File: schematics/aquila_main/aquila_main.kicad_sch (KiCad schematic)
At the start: 126 parts

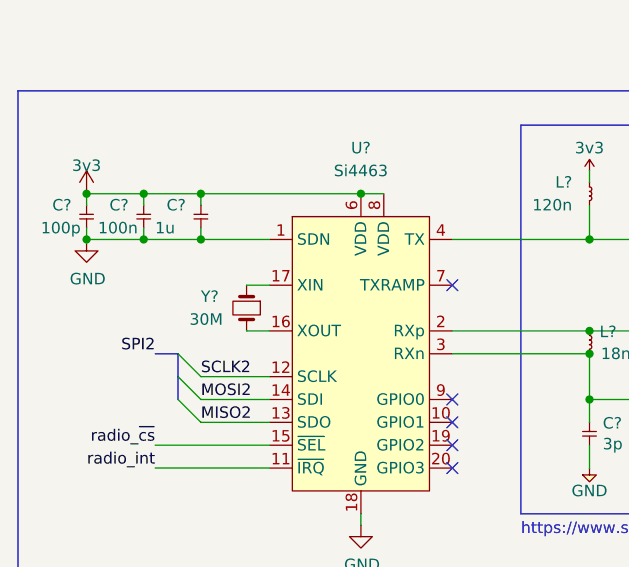
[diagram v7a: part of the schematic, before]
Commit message: added footprint for crystal
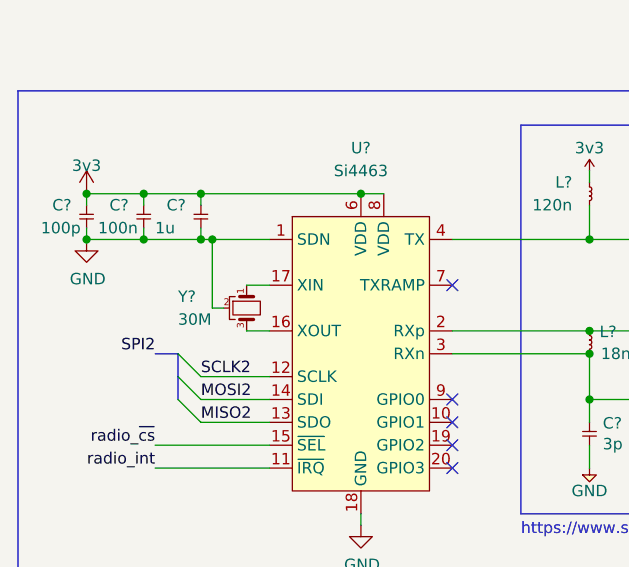
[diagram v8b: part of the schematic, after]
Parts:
- removed Y?: 30M, symbol Device:Crystal_Small
- added Y?: 30M, symbol Device:Crystal_GND2_Small
- J?: Farnell (none) -> 1216976; farnell 1216976 -> (none)
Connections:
- net GND: now also Y?.2
- net at U?.17 (XIN): now also Y?.1
- net at U?.16 (XOUT): now also Y?.3
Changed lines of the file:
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@@
   (junction (at 297.18 200.66) (diameter 0) (color 0 0 0 0)
   )
+  (junction (at 69.85 162.56) (diameter 0) (color 0 0 0 0)
+  )
   (junction (at 242.57 184.15) (diameter 0) (color 0 0 0 0)
   )
@@
     (stroke (width 0) (type default) (color 0 0 0 0))
   )
-  (wire (pts (xy 76.2 162.56) (xy 68.58 162.56))
+  (wire (pts (xy 76.2 162.56) (xy 69.85 162.56))
     (stroke (width 0) (type default) (color 0 0 0 0))
   )
@@
     (stroke (width 0) (type default) (color 0 0 0 0))
   )
+  (wire (pts (xy 71.12 170.18) (xy 69.85 170.18))
+    (stroke (width 0) (type default) (color 0 0 0 0))
+  )
   (wire (pts (xy 264.16 208.28) (xy 242.57 208.28))
     (stroke (width 0) (type default) (color 0 0 0 0))
@@
     (stroke (width 0) (type default) (color 0 0 0 0))
   )
+  (wire (pts (xy 69.85 162.56) (xy 68.58 162.56))
+    (stroke (width 0) (type default) (color 0 0 0 0))
+  )
   (wire (pts (xy 302.26 187.96) (xy 302.26 189.23))
     (stroke (width 0) (type default) (color 0 0 0 0))
@@
     (stroke (width 0) (type default) (color 0 0 0 0))
   )
+  (wire (pts (xy 69.85 162.56) (xy 69.85 170.18))
+    (stroke (width 0) (type default) (color 0 0 0 0))
+  )
   (wire (pts (xy 176.53 58.42) (xy 179.07 58.42))
     (stroke (width 0) (type default) (color 0 0 0 0))
@@
     (pin "2")
   )
-  (symbol (lib_id "Device:Crystal_Small") (at 73.66 170.18 90) (mirror x) (unit 1)
-    (in_bom yes) (on_board yes)
-    (property "Reference" "Y?" (id 0) (at 68.58 168.91 90)
-      (effects (font (size 1.27 1.27)) (justify right))
-    )
-    (property "Value" "30M" (id 1) (at 67.31 171.45 90)
-      (effects (font (size 1.27 1.27)) (justify right))
-    )
-    (property "Footprint" "" (id 2) (at 73.66 170.18 0)
-      (effects (font (size 1.27 1.27)) hide)
-    )
-    (property "Datasheet" "~" (id 3) (at 73.66 170.18 0)
-      (effects (font (size 1.27 1.27)) hide)
-    )
-    (pin "1")
-    (pin "2")
-  )
   (symbol (lib_id "aquila:C-cusf-kicad") (at 68.58 158.75 270) (unit 1)
     (in_bom yes) (on_board yes)
@@
     (pin "1")
   )
+  (symbol (lib_id "Device:Crystal_GND2_Small") (at 73.66 170.18 270) (unit 1)
+    (in_bom yes) (on_board yes)
+    (property "Reference" "Y?" (id 0) (at 66.04 168.91 90)
+      (effects (font (size 1.27 1.27)) (justify left))
+    )
+    (property "Value" "30M" (id 1) (at 66.04 171.45 90)
+      (effects (font (size 1.27 1.27)) (justify left))
+    )
+    (property "Footprint" "" (id 2) (at 73.66 170.18 0)
+      (effects (font (size 1.27 1.27)) hide)
+    )
+    (property "Datasheet" "~" (id 3) (at 73.66 170.18 0)
+      (effects (font (size 1.27 1.27)) hide)
+    )
+    (pin "1")
+    (pin "2")
+    (pin "3")
+  )
   (symbol (lib_id "aquila:BMI-S-201") (at 252.73 243.84 0) (unit 1)
     (in_bom yes) (on_board yes)
@@
       (effects (font (size 1.27 1.27)) hide)
     )
-    (property "farnell" "1216976" (id 4) (at 368.3 177.8 0)
+    (property "Farnell" "1216976" (id 4) (at 368.3 177.8 0)
       (effects (font (size 1.27 1.27)) hide)
     )
@@
       (reference "U?") (unit 1) (value "MAX-M8Q") (footprint "aquila:MAX-M8Q")
     )
-    (path "/00000000-0000-0000-0000-0000623ab755"
+    (path "/5261fde7-e5b4-4565-991d-43c69ff8ae8d"
       (reference "Y?") (unit 1) (value "30M") (footprint "")
     )
